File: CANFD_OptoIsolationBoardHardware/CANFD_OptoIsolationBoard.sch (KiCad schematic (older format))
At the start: 30 parts, among them CN1 CONN_8X2, CN2 CONN_3, CN3 DB9, U1 MCP2517FD, U2 MAX22245, U3 MAX22245, U4 MCP2562FD, U5 RFMM-0505S, X1 50MHz

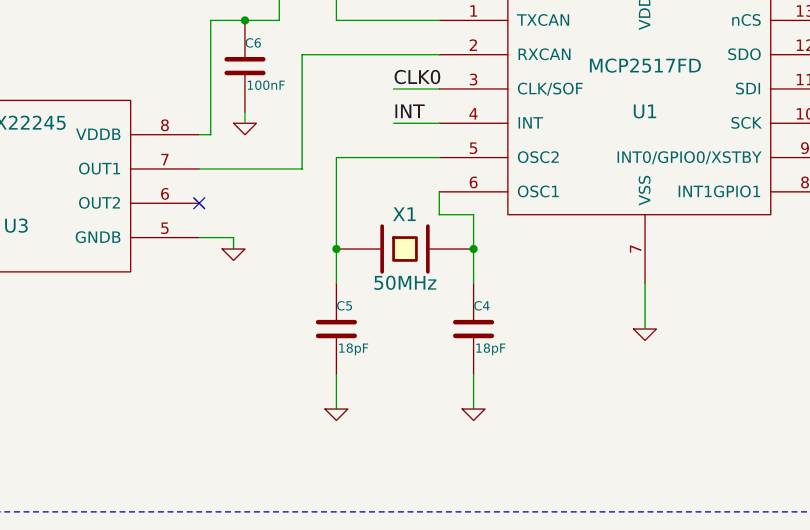
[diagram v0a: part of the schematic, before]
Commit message: Update quartz information
Previous value of quartz was incorrect(50MHz) now value is correct(40MHz)
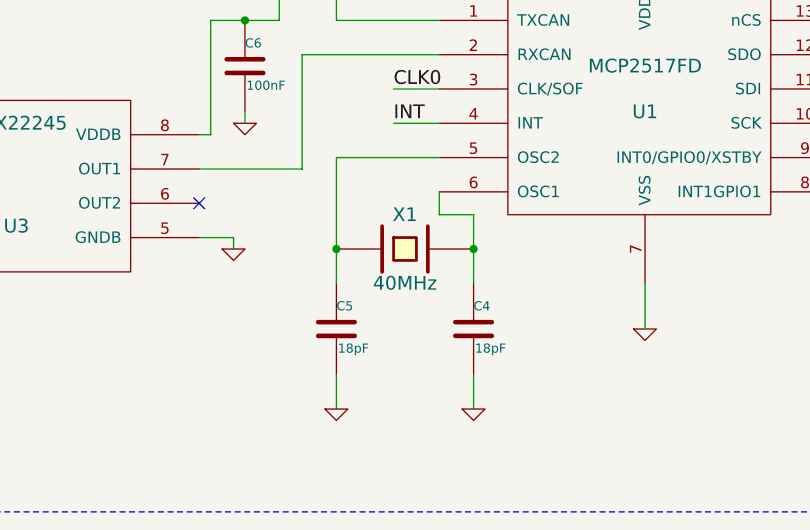
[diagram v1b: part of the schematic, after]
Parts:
- X1: value 50MHz -> 40MHz
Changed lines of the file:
@@
 Sheet 1 1
 Title "CANFD_OptoIsolationBoard.sch"
-Date "10 dec 2021"
+Date "2 apr 2022"
 Rev ""
 Comp ""
@@
 P 8400 5450
 F 0 "X1" H 8400 5600 60  0000 C CNN
-F 1 "50MHz" H 8400 5300 60  0000 C CNN
+F 1 "40MHz" H 8400 5300 60  0000 C CNN
 F 2 "~" H 8400 5450 60  0000 C CNN
 F 3 "~" H 8400 5450 60  0000 C CNN
